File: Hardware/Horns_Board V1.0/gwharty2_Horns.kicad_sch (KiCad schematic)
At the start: 17 parts, among them J1 Conn_01x03, J2 Conn_01x02, J3 Conn_01x02, J4 Conn_01x02, Q1 STD7NK40Z

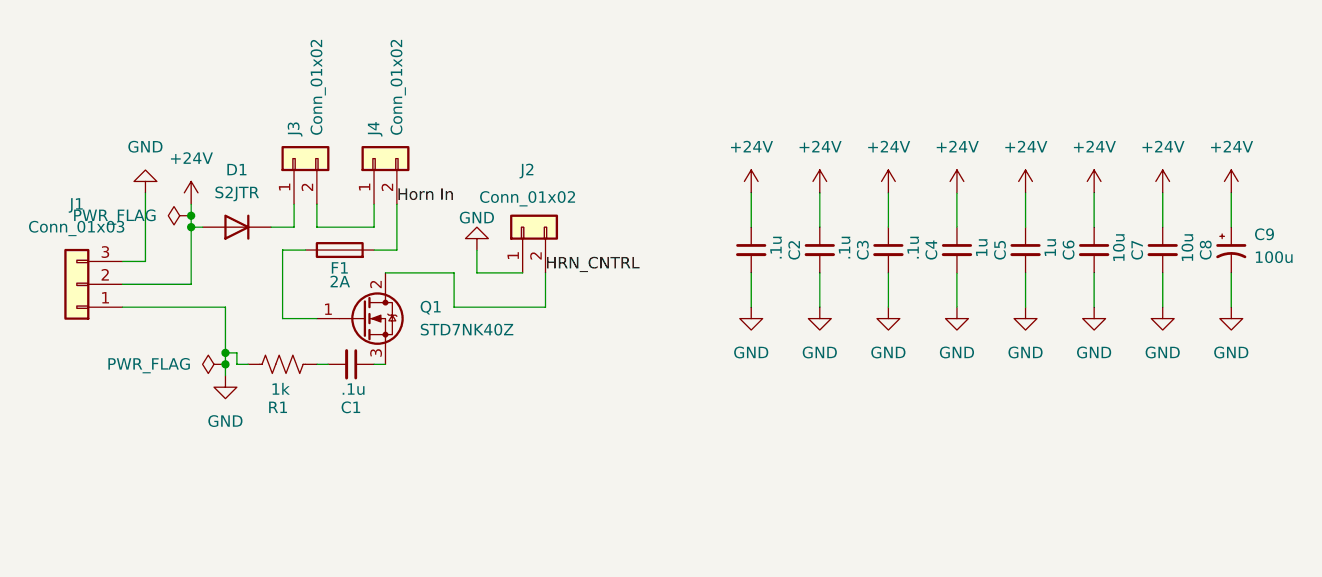
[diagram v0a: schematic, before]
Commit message: updated horn schematic
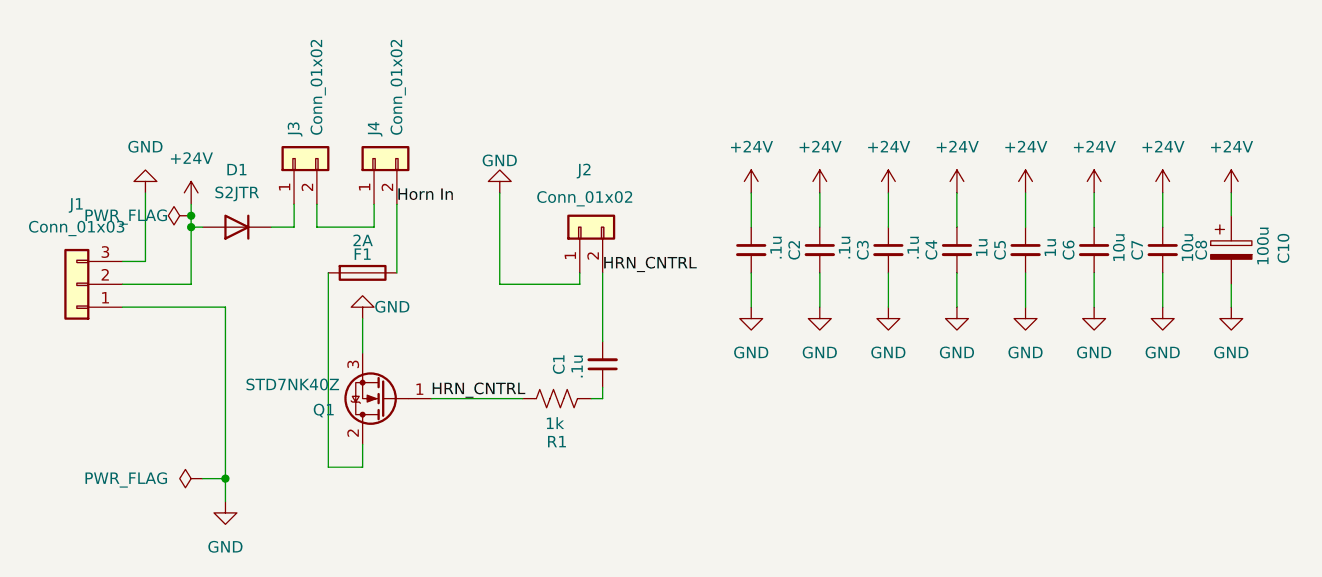
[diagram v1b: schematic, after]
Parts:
- removed C9: 100u, symbol device:C_Polarized_Small_US
- added C10: 100u, symbol device:C_Polarized
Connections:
- net +24V: now also C10.1
- net GND: now also Q1.3 (S), C10.2; no longer R1.1
- net HRN_CNTRL: now also C1.2, Q1.1 (G), R1.1; no longer Q1.2 (D)
- net Horn In: now also F1.1; no longer F1.2
- net at R1.2: now also C1.1; no longer C1.2
- new net: F1.2, Q1.2 (D)
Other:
- moved on the sheet: C1, F1, J2, Q1, R1

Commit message: updated horns PCB (passed DRC)
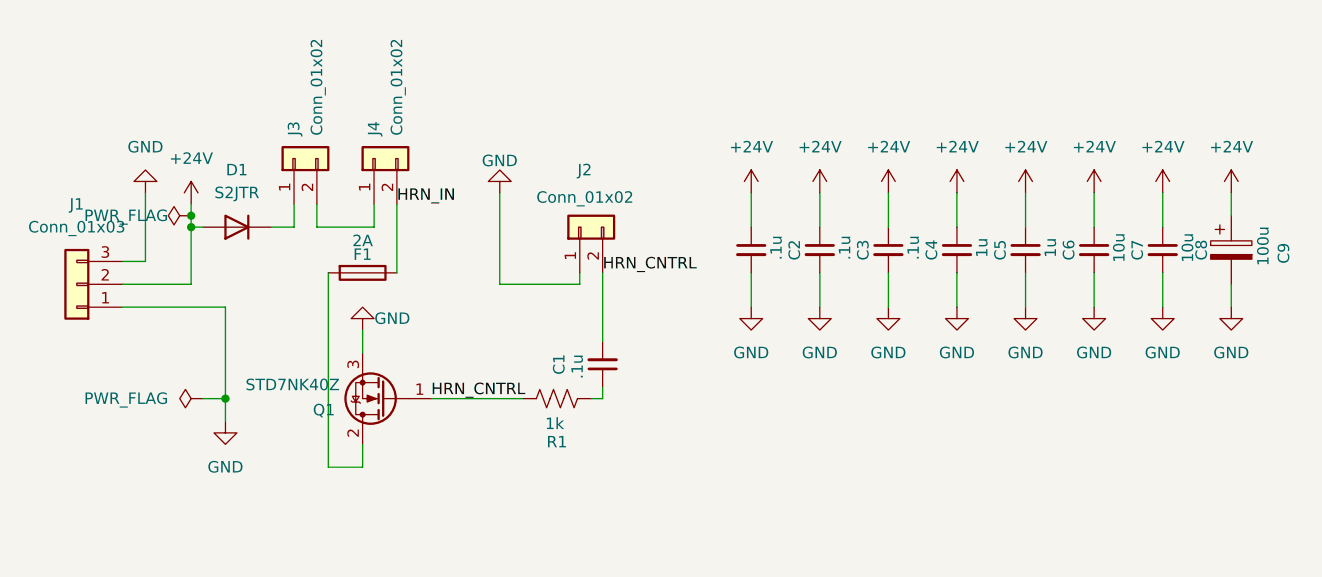
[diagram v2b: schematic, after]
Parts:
- C1, C2, C3, C4, C5, C6, C7, C8: footprint (none) -> Capacitor_SMD:C_0603_1608Metric_Pad1.08x0.95mm_HandSolder
- C9: renamed from C10; footprint (none) -> Capacitor_SMD:C_Elec_3x5.4; Notes (none) -> Might change out not sure of standard
- F1: footprint (none) -> Fuse:Fuse_0603_1608Metric_Pad1.05x0.95mm_HandSolder
- J1: footprint (none) -> Connector_Molex:Molex_KK-254_AE-6410-03A_1x03_P2.54mm_Vertical
- J2, J3, J4: footprint (none) -> Connector_Molex:Molex_KK-254_AE-6410-02A_1x02_P2.54mm_Vertical
- R1: footprint (none) -> Resistor_SMD:R_0603_1608Metric_Pad0.98x0.95mm_HandSolder
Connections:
- net Horn In renamed HRN_IN
